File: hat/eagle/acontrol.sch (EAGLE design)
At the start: 8 parts, among them J1 RASPBERRYPI-40-PIN-GPIO_PTH_N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, J4 4P-2.0-90D, J5 GREEN-2P-3.5, J7 455-1750-1-ND, U1 TXB0104

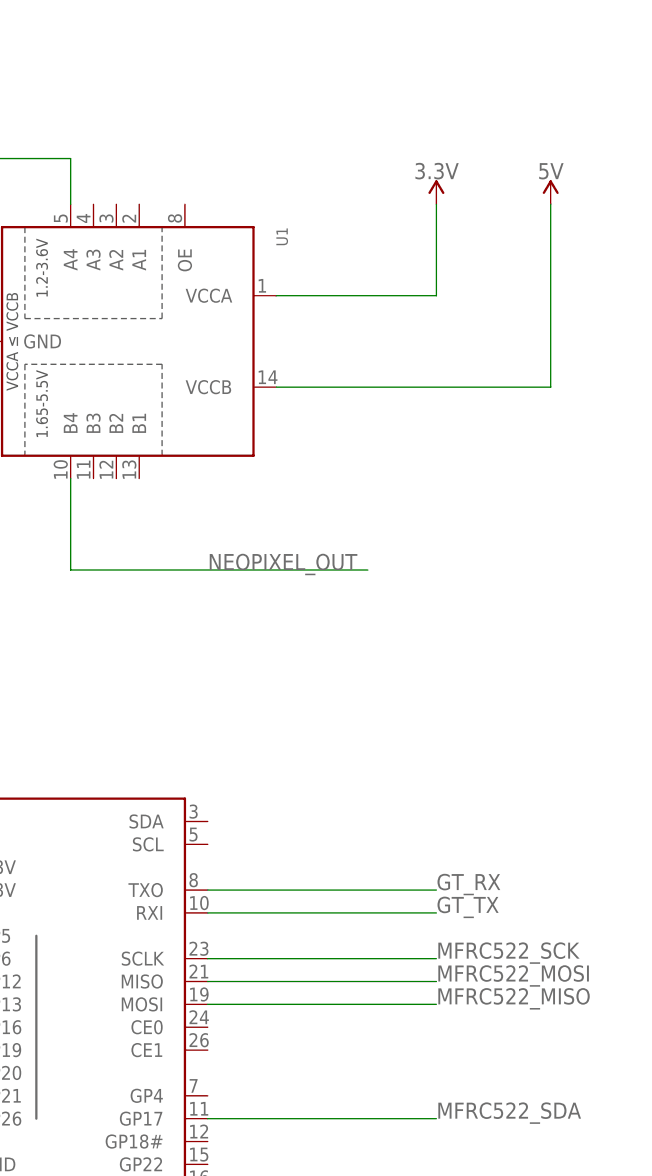
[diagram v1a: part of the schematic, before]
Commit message: uHat corrections + 3D printed case
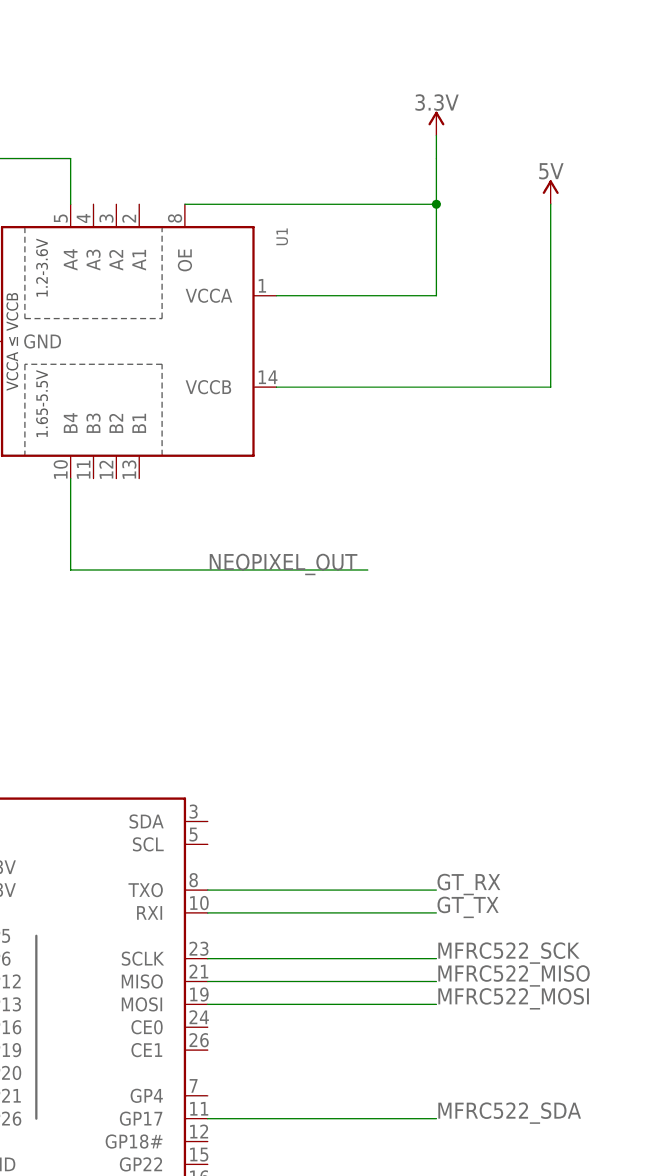
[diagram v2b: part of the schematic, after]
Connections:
- net 3.3V: now also U1.OE
- net MFRC522_MISO: now also J1.MISO; no longer J1.MOSI
- net MFRC522_MOSI: now also J1.MOSI; no longer J1.MISO
